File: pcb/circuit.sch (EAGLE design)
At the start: 148 parts, among them IC1 MCP1612-ADJI/MS, IC2 MCP73833-AMI/UN-ND, IC3 WE-TVS, IC4 MCP3423, IC5 ATWINC1510-MR210PB1952-ND, IC6 MAX3378EEUD, IC7 RN4870, IC8 ATSAML22N18A, J1 22-05-7038-03, J10 2.5MM-AUDIO-JACK-MONONO_DRILL, J11 2.5MM-AUDIO-JACK-MONONO_DRILL, J12 2.5MM-AUDIO-JACK-MONONO_DRILL, J13 2.5MM-AUDIO-JACK-MONONO_DRILL, J2 USB2-MICRO, J3 2.5MM-AUDIO-JACK-MONO, J4 2.5MM-AUDIO-JACK-MONO, J5 2.5MM-AUDIO-JACK-MONO, J6 2.5MM-AUDIO-JACK-MONO, J7 2.5MM-AUDIO-JACK-MONO, J8 22-05-7028-02, J9 2.5MM-AUDIO-JACK-MONONO_DRILL, Q1 ECX-1210, T1 PMOS, T10 NMOSSOT323, T11 NMOSSOT323, T12 NMOSSOT323, T2 NMOSSOT323, T3 NMOSSOT323, T4 NMOSSOT323, T5 NMOSSOT323, T6 NMOSSOT323, T7 NMOSSOT323, T8 NMOSSOT323, T9 NMOSSOT323, X1 B3S-1000, X2 MOLEX_1MM_FPC, X3 IGRID-20

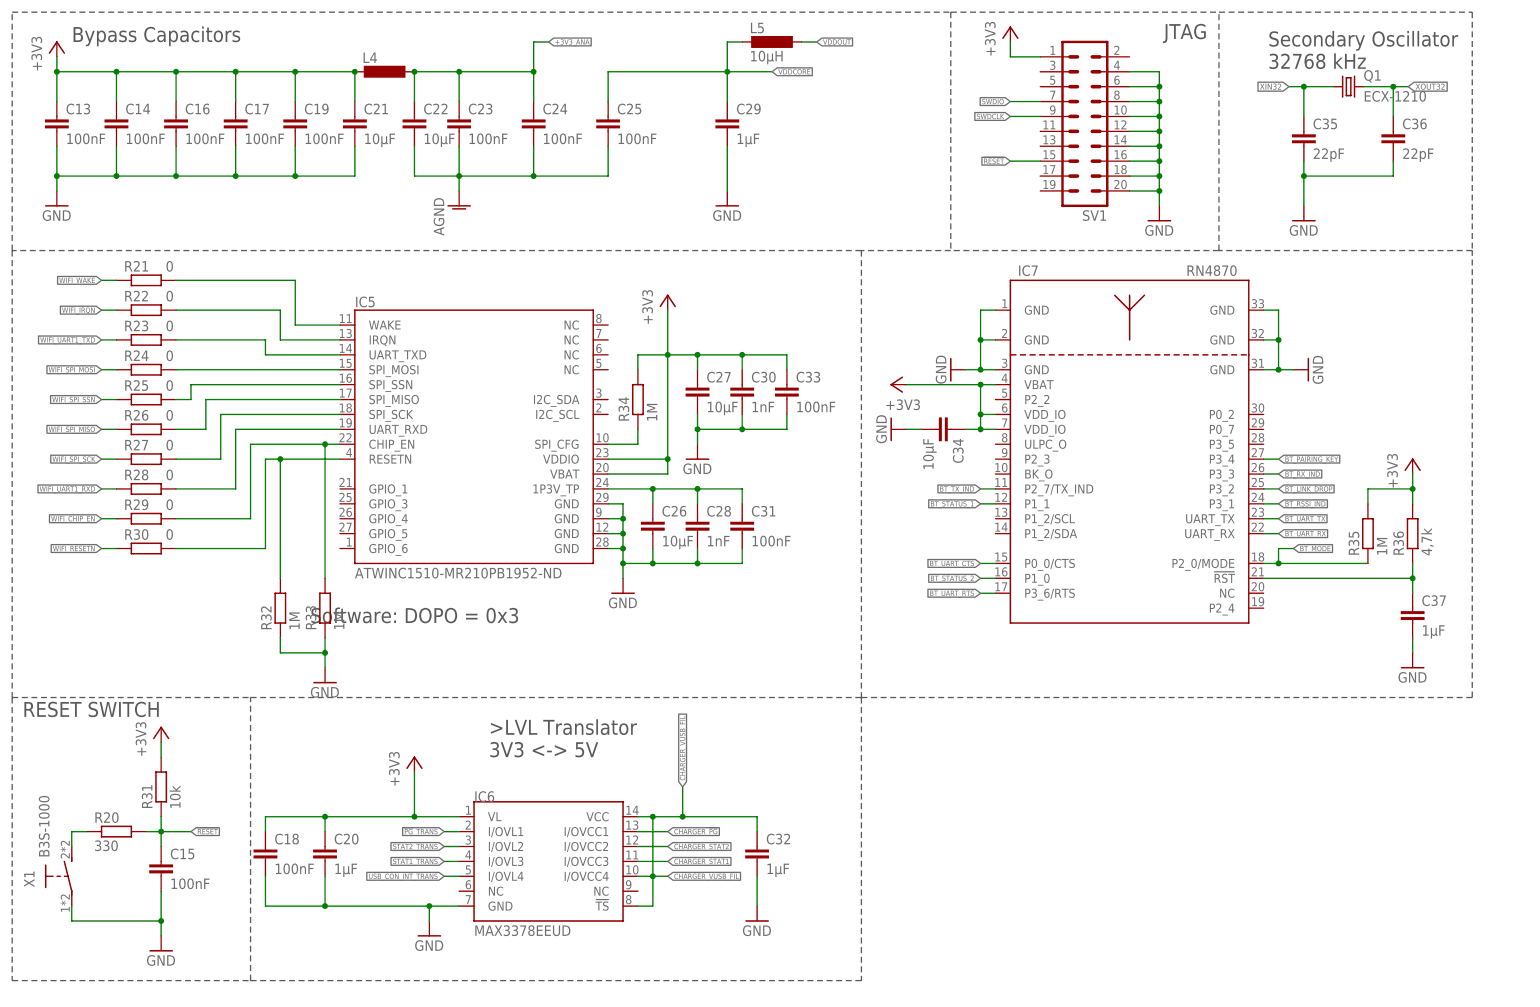
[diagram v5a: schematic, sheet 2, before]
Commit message: Power Unit
-power unit routed
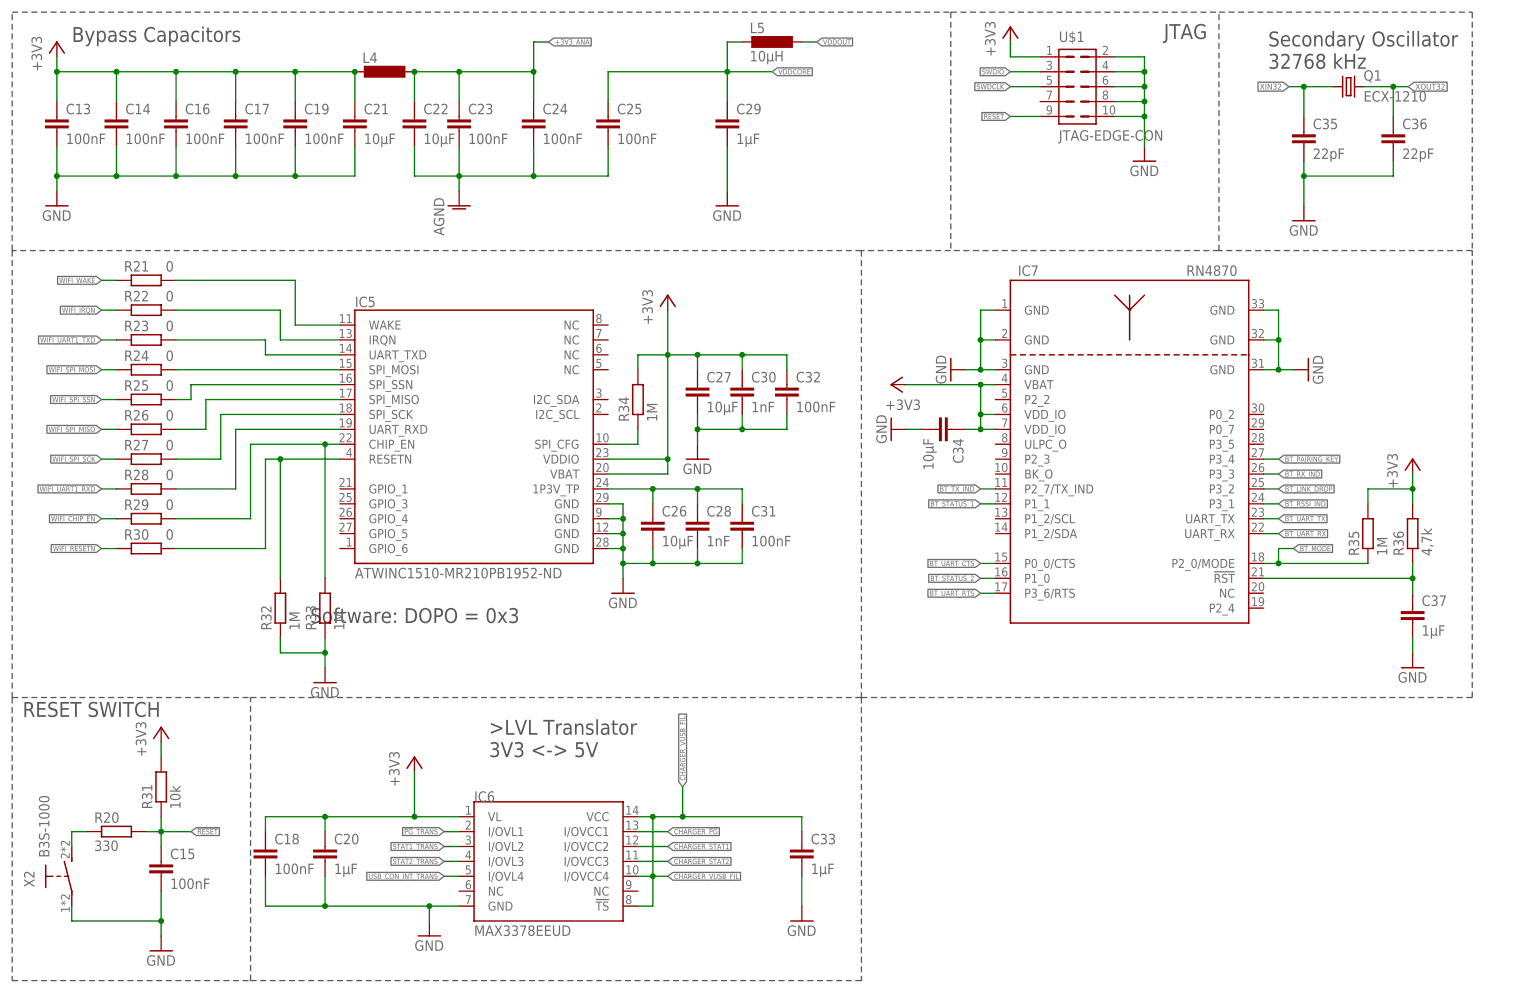
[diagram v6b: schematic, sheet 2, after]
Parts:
- removed J3, J4, J5, J6, J7: 2.5MM-AUDIO-JACK-MONO, Thermo_Library:2.5MM-AUDIO-JACK-MONO
- removed J8: 22-05-7028-02, con-molex:22-05-7028-02
- removed SV1: JTAGEDU, con-harting-ml:ML20
- added U$1: JTAG-EDGE-CON, thermo:JTAG-EDGE-CON
- added X14: MOLEX_1MM_FPC, thermo:MOLEX_1MM_FPC
- added X4, X5, X6, X7, X8: 2.5MM-AUDIO-JACK-MONODRILL, thermo:2.5MM-AUDIO-JACK-MONODRILL
- C32: value 1µF -> 100nF; OC_MOUSER 810-CGA3E1X7R1E105AC -> 581-06033C104KAT2A
- C33: value 100nF -> 1µF; OC_MOUSER 581-06033C104KAT2A -> 810-CGA3E1X7R1E105AC
- J2: value USB2-MICRO -> 22-05-7038-03; device thermo:USB2-MICRO -> con-molex:22-05-7038-03; OC_MOUSER 649-10104110-0001LF -> (none)
- JP1, JP2, JP6, JP7: value 4 -> (none); device jumper:JP4E -> thermo:JP4; OC_MOUSER 855-M20-9770446 -> (none)
- JP3, JP4: value 2 -> (none); device jumper:JP1E -> thermo:JP2; OC_MOUSER 855-M20-9990246 -> (none)
- JP5: value 3 -> (none); device jumper:JP2E -> thermo:JP3; OC_FARNELL 710-61300311121 -> (none)
- X1: value B3S-1000 -> USB2-MICRO; device Thermo_Library:B3S-1000 -> thermo:USB2-MICRO; OC_MOUSER 653-B3S-1000 -> (none)
- X2: value MOLEX_1MM_FPC -> B3S-1000; device thermo:MOLEX_1MM_FPC -> Thermo_Library:B3S-1000; OC_MOUSER (none) -> 653-B3S-1000
- renumbered J10 to X10, J11 to X11, J12 to X12, J13 to X13, J9 to X9, X3 to X15
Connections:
- net !RESET!: now also U$1.9; no longer SV1.15
- net !RESET!_B: now also X2.S; no longer X1.S
- net +3V3: now also C32.1, U$1.1, X14.1; no longer C33.1, SV1.1, X2.1
- net +3V3_ANA: now also X4.2, X5.2, X6.2, X7.2, X8.2; no longer J3.2, J4.2, J5.2, J6.2, J7.2
- net CHARGER_STAT1: now also IC6.I/OVCC2; no longer IC6.I/OVCC3
- net CHARGER_STAT2: now also IC6.I/OVCC3; no longer IC6.I/OVCC2
- net CHARGER_VUSB_FIL: now also C33.1; no longer C32.1
- net EXT_PWM_0: now also J2-1.S; no longer J8-1.S
- net EXT_PWM_1: now also J2-2.S; no longer J8-2.S
- net GND: now also J2-3.S, U$1.10, U$1.2, U$1.4, U$1.6, U$1.8, X1.GND, X14.6, X2.P; no longer J2.GND, SV1.10, SV1.12, SV1.14, SV1.16, SV1.18, SV1.20, SV1.4, SV1.6, SV1.8, X1.P, X2.6
- net SENSOR_INT_0: now also X4.3; no longer J3.3
- net SENSOR_INT_1: now also X5.3; no longer J4.3
- net SENSOR_INT_2: now also X6.3; no longer J5.3
- net SENSOR_INT_3: now also X7.3; no longer J6.3
- net SENSOR_INT_4: now also X8.3; no longer J7.3
- net SENSOR_IN_0: now also X4.1; no longer J3.1
- net SENSOR_IN_1: now also X5.1; no longer J4.1
- net SENSOR_IN_2: now also X6.1; no longer J5.1
- net SENSOR_IN_3: now also X7.1; no longer J6.1
- net SENSOR_IN_4: now also X8.1; no longer J7.1
- net STAT1_TRANS: now also IC6.I/OVL2; no longer IC6.I/OVL3
- net STAT2_TRANS: now also IC6.I/OVL3; no longer IC6.I/OVL2
- net SWDCLK: now also U$1.5; no longer SV1.9
- net SWDIO: now also U$1.3; no longer SV1.7
- net UI_BUTTON_INT_0: now also X14.2; no longer X2.2
- net UI_BUTTON_INT_1: now also X14.3; no longer X2.3
- net UI_BUTTON_INT_2: now also X14.4; no longer X2.4
- net UI_BUTTON_INT_3: now also X14.5; no longer X2.5
- net USB_D_N: now also X1.D-; no longer J2.D-
- net USB_D_P: now also X1.D+; no longer J2.D+
- net USB_SHIELD: now also X1.SHIELD; no longer J2.SHIELD
- net USB_VCC: now also X1.VCC; no longer J2.VCC
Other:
- moved on the sheet: C32, C33

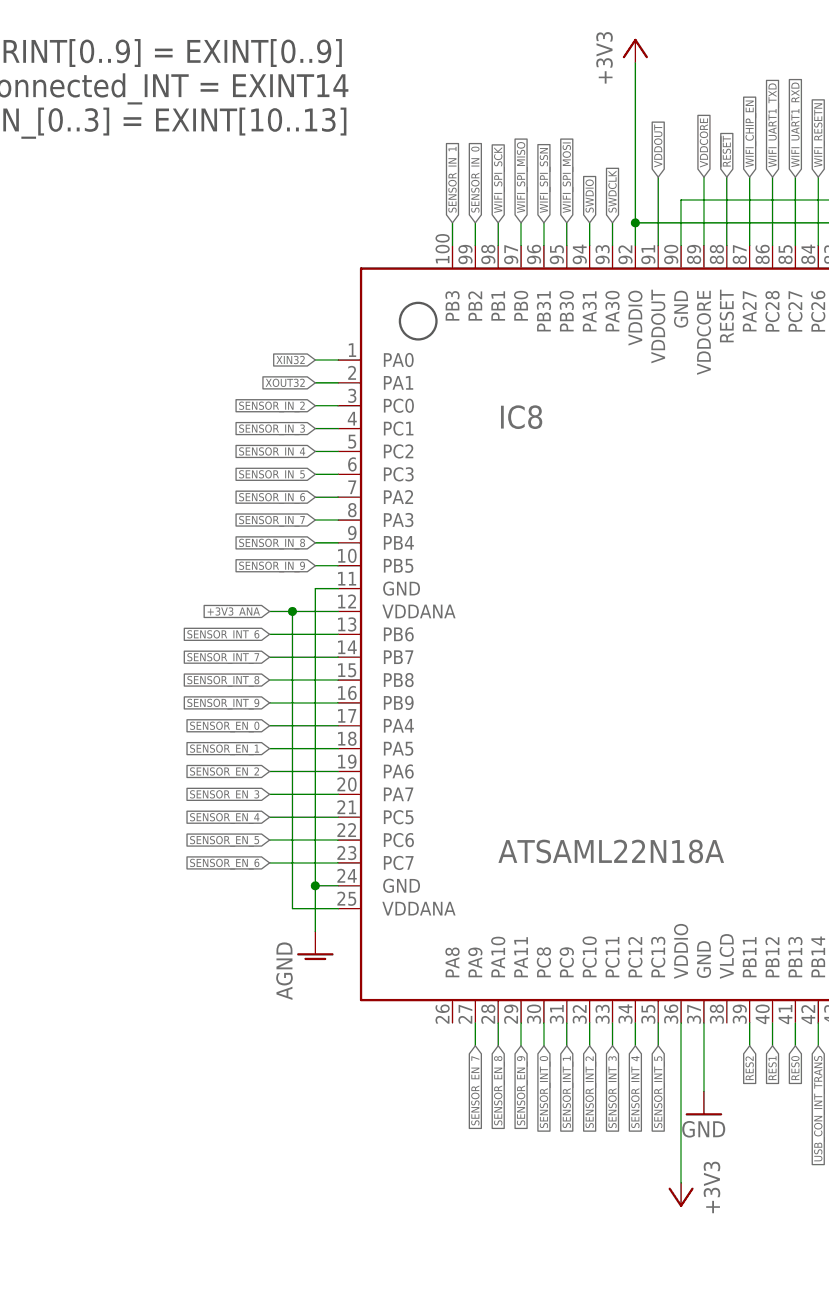
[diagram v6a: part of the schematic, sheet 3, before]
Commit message: Senor Pinout refactored
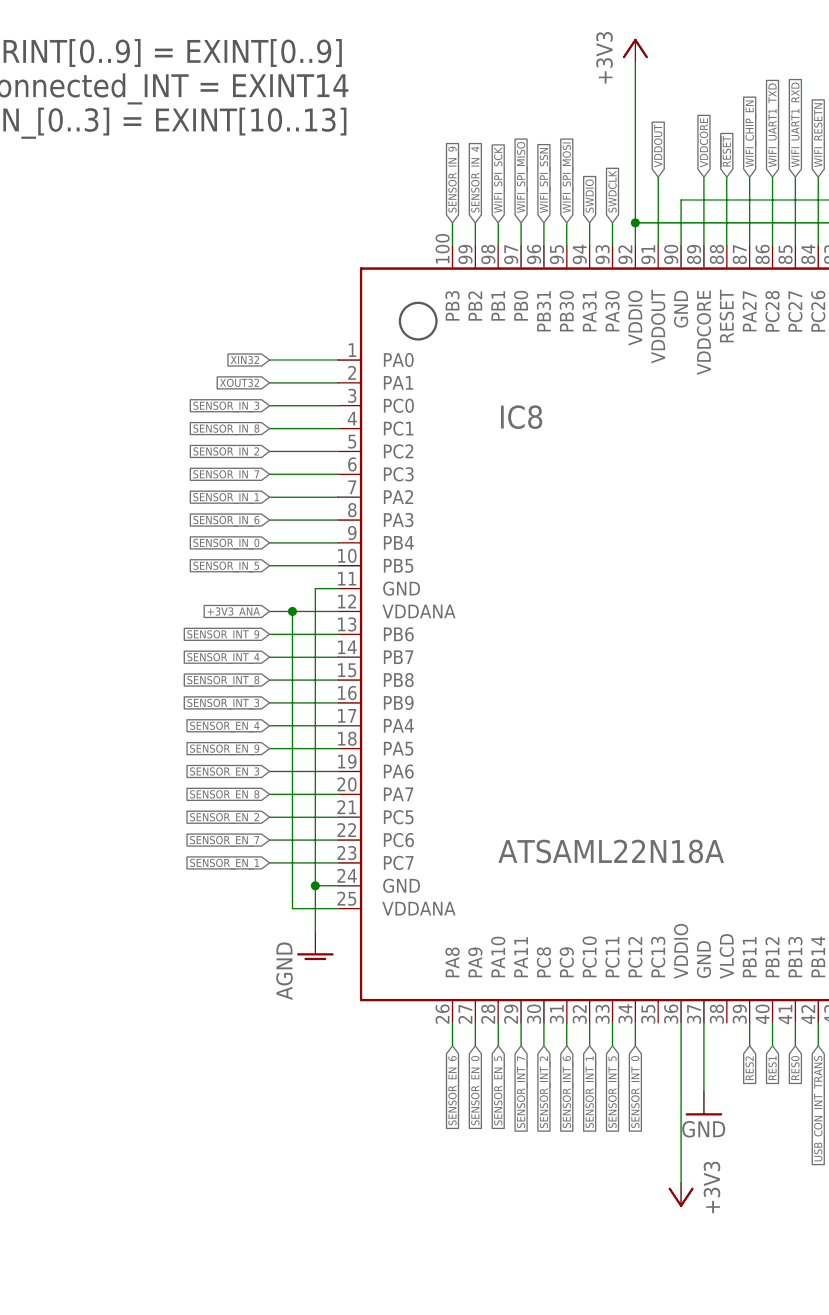
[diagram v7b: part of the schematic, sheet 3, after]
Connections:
- net !RESET!: now also U$1.3; no longer U$1.9
- net +3V3: now also U$1.5; no longer U$1.1
- net GND: now also U$1.7, U$1.9; no longer U$1.2, U$1.4
- net SENSOR_EN_0: now also IC8.PA9; no longer IC8.PA4
- net SENSOR_EN_1: now also IC8.PC7; no longer IC8.PA5
- net SENSOR_EN_2: now also IC8.PC5; no longer IC8.PA6
- net SENSOR_EN_3: now also IC8.PA6; no longer IC8.PA7
- net SENSOR_EN_4: now also IC8.PA4; no longer IC8.PC5
- net SENSOR_EN_5: now also IC8.PA10; no longer IC8.PC6
- net SENSOR_EN_6: now also IC8.PA8; no longer IC8.PC7
- net SENSOR_EN_7: now also IC8.PC6; no longer IC8.PA9
- net SENSOR_EN_8: now also IC8.PA7; no longer IC8.PA10
- net SENSOR_EN_9: now also IC8.PA5; no longer IC8.PA11
- net SENSOR_INT_0: now also IC8.PC12; no longer IC8.PC8
- net SENSOR_INT_1: now also IC8.PC10; no longer IC8.PC9
- net SENSOR_INT_2: now also IC8.PC8; no longer IC8.PC10
- net SENSOR_INT_3: now also IC8.PB9; no longer IC8.PC11
- net SENSOR_INT_4: now also IC8.PB7; no longer IC8.PC12
- net SENSOR_INT_5: now also IC8.PC11; no longer IC8.PC13
- net SENSOR_INT_6: now also IC8.PC9; no longer IC8.PB6
- net SENSOR_INT_7: now also IC8.PA11; no longer IC8.PB7
- net SENSOR_INT_9: now also IC8.PB6; no longer IC8.PB9
- net SENSOR_IN_0: now also IC8.PB4; no longer IC8.PB2
- net SENSOR_IN_1: now also IC8.PA2; no longer IC8.PB3
- net SENSOR_IN_2: now also IC8.PC2; no longer IC8.PC0
- net SENSOR_IN_3: now also IC8.PC0; no longer IC8.PC1
- net SENSOR_IN_4: now also IC8.PB2; no longer IC8.PC2
- net SENSOR_IN_5: now also IC8.PB5; no longer IC8.PC3
- net SENSOR_IN_6: now also IC8.PA3; no longer IC8.PA2
- net SENSOR_IN_7: now also IC8.PC3; no longer IC8.PA3
- net SENSOR_IN_8: now also IC8.PC1; no longer IC8.PB4
- net SENSOR_IN_9: now also IC8.PB3; no longer IC8.PB5
- net SWDCLK: now also U$1.2; no longer U$1.5
- net SWDIO: now also U$1.1; no longer U$1.3

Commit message: routed RN4970
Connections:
- net !PG!_TRANS: now also IC6.I/OVL2; no longer IC6.I/OVL1
- net BT_MODE: now also IC8.PA21; no longer IC8.PB19
- net BT_PAIRING_KEY: now also IC8.PB19; no longer IC8.PA21
- net BT_RSSI_IND: now also IC8.PA20; no longer IC8.PB20
- net BT_RX_IND: now also IC8.PB20; no longer IC8.PA20
- net CHARGER_!PG!: now also IC6.I/OVCC2; no longer IC6.I/OVCC1
- net CHARGER_STAT1: now also IC6.I/OVCC3; no longer IC6.I/OVCC2
- net CHARGER_STAT2: now also IC6.I/OVCC4; no longer IC6.I/OVCC3
- net CHARGER_VUSB_FIL: now also IC6.I/OVCC1; no longer IC6.I/OVCC4
- net OLED_D/C: now also IC8.PB15; no longer IC8.PC14
- net OLED_EN: now also IC8.PC14; no longer IC8.PB15
- net SENSOR_EN_2: now also IC8.PC6; no longer IC8.PC5
- net SENSOR_EN_3: now also IC8.PA7; no longer IC8.PA6
- net SENSOR_EN_7: now also IC8.PC5; no longer IC8.PC6
- net SENSOR_EN_8: now also IC8.PA6; no longer IC8.PA7
- net STAT1_TRANS: now also IC6.I/OVL3; no longer IC6.I/OVL2
- net STAT2_TRANS: now also IC6.I/OVL4; no longer IC6.I/OVL3
- net USB_CON_INT_TRANS: now also IC6.I/OVL1; no longer IC6.I/OVL4
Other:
- moved on the sheet: IC6
